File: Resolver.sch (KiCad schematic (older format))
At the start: 10 parts, among them U6 AD2S1200YSTZ, Y2 8.912 MHZ

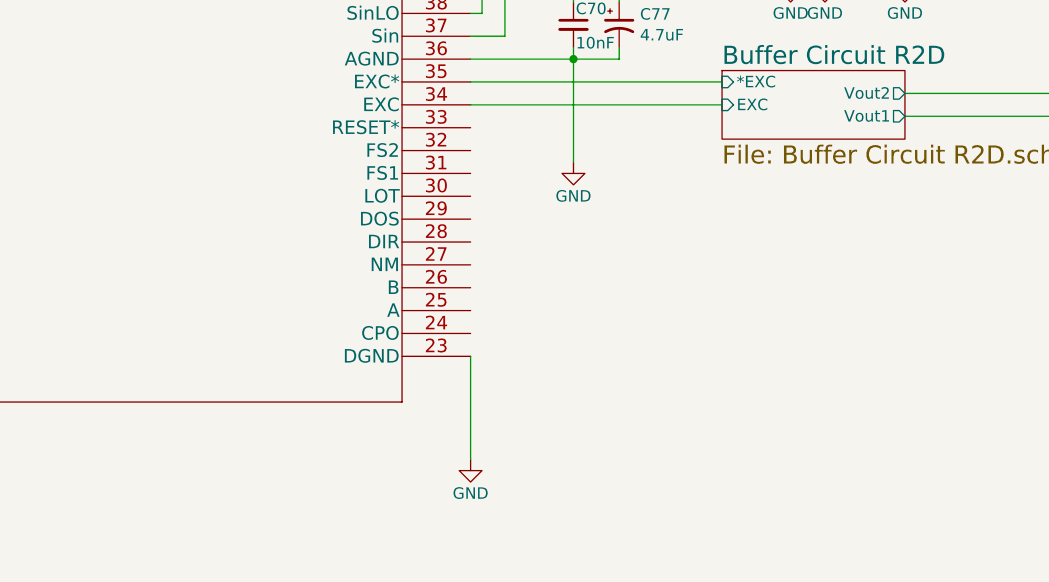
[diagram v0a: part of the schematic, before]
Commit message: continued R2D AS1200 has encoder-interface
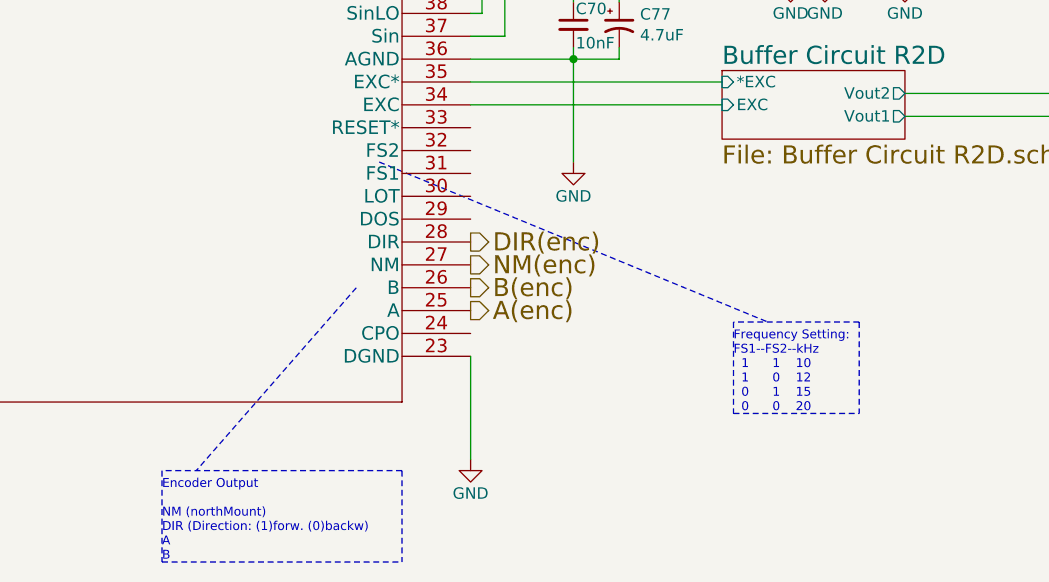
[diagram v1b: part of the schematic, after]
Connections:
- net A(enc): now reaches U6.25 (A)
- net B(enc): now reaches U6.26 (B)
- net NM(enc): now reaches U6.27 (NM)
- net DIR(enc): now reaches U6.28 (DIR)
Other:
- note added: "Encoder Output\n\nNM (northMount)\nDIR (Direction: (1)forw. (0)backw)\nA\nB"
- note added: "Frequency Setting:\nFS1--FS2--kHz\n 1 1 10\n 1 0 12\n 0 1 15\n 0 0 20"
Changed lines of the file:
@@
 P 5850 5350
 AR Path="/5895E6A0/5CAF8D8E" Ref="#PWR?"  Part="1"
-AR Path="/5C9D0FFC/5CAF8D8E" Ref="#PWR?"  Part="1"
-F 0 "#PWR?" H 5850 5100 50  0001 C CNN
+AR Path="/5C9D0FFC/5CAF8D8E" Ref="#PWR0138"  Part="1"
+F 0 "#PWR0138" H 5850 5100 50  0001 C CNN
 F 1 "GND" H 5850 5200 50  0000 C CNN
 F 2 "" H 5850 5350 50  0000 C CNN
@@
 Wire Wire Line
 	2150 3200 2850 3200
+Text Notes 7000 5150 0    39   ~ 0
+Frequency Setting:\nFS1--FS2--kHz\n  1      1    10\n  1      0    12\n  0      1    15\n  0      0    20
+Wire Notes Line
+	5450 4050 7150 4750
+Wire Notes Line
+	7000 5150 7550 5150
+Wire Notes Line
+	7550 4750 7000 4750
+Wire Notes Line
+	7000 4750 7000 5150
+Wire Notes Line
+	7550 4750 7550 5150
+Text Notes 4500 5800 0    39   ~ 0
+Encoder Output\n\nNM (northMount)\nDIR (Direction: (1)forw. (0)backw)\nA\nB
+Wire Notes Line
+	5350 4600 4650 5400
+Wire Notes Line
+	4500 5800 5550 5800
+Wire Notes Line
+	5550 5400 4500 5400
+Wire Notes Line
+	4500 5400 4500 5800
+Wire Notes Line
+	5550 5400 5550 5800
+Text HLabel 5850 4600 2    79   Output ~ 0
+B(enc)
+Text HLabel 5850 4500 2    79   Output ~ 0
+NM(enc)
+Text HLabel 5850 4400 2    79   Output ~ 0
+DIR(enc)
+Text HLabel 5850 4700 2    79   Output ~ 0
+A(enc)
 $EndSCHEMATC

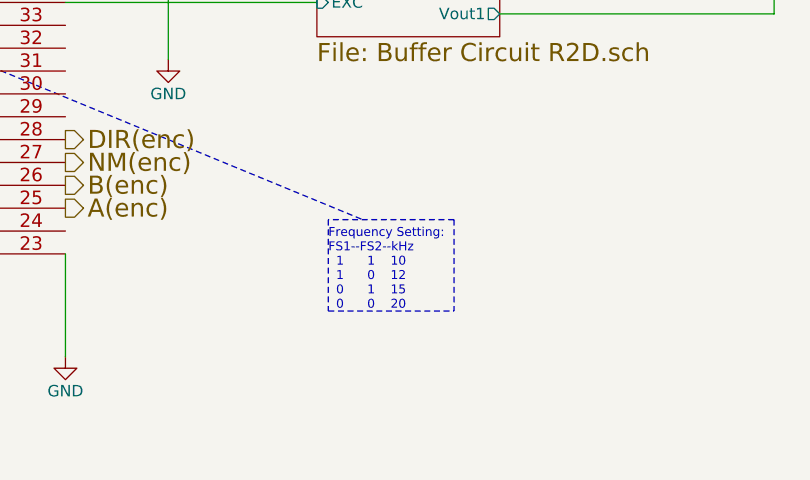
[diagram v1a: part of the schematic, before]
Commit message: continued Resolver continued Routing
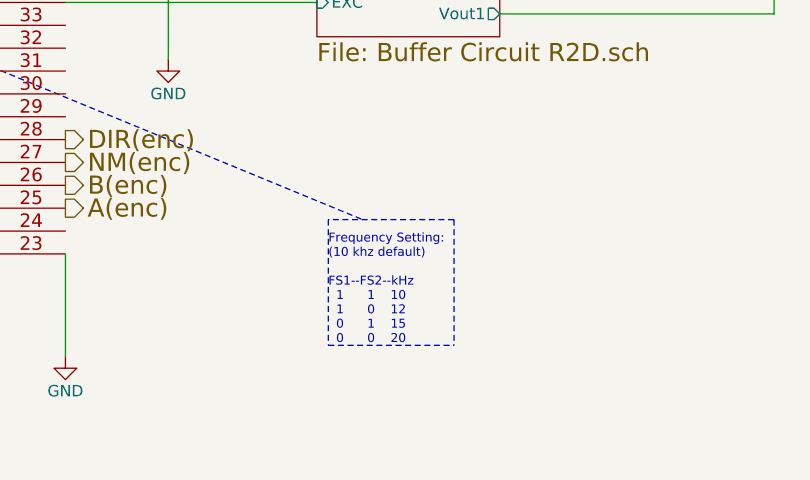
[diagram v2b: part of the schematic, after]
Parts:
- C74, C77: footprint Capacitor_SMD:C_0805_2012Metric -> Capacitor_Tantalum_SMD:CP_EIA-3216-12_Kemet-S
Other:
- note added: "Frequency Setting:\n(10 khz default)\n\nFS1--FS2--kHz\n 1 1 10\n 1 0 12\n 0 1 15\n 0 0 20"
- note removed: "Frequency Setting:\nFS1--FS2--kHz\n 1 1 10\n 1 0 12\n 0 1 15\n 0 0 20"
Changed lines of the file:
@@
 $Descr A4 11693 8268
 encoding utf-8
-Sheet 8 10
+Sheet 9 10
 Title ""
 Date ""
@@
 F 0 "C77" H 6591 3496 50  0000 L CNN
 F 1 "4.7uF" H 6591 3405 50  0000 L CNN
-F 2 "Capacitor_SMD:C_0805_2012Metric" H 6500 3450 50  0001 C CNN
+F 2 "Capacitor_Tantalum_SMD:CP_EIA-3216-12_Kemet-S" H 6500 3450 50  0001 C CNN
 F 3 "~" H 6500 3450 50  0001 C CNN
 	1    6500 3450
@@
 F 0 "C74" H 1441 4596 50  0000 L CNN
 F 1 "4.7uF" H 1441 4505 50  0000 L CNN
-F 2 "Capacitor_SMD:C_0805_2012Metric" H 1350 4550 50  0001 C CNN
+F 2 "Capacitor_Tantalum_SMD:CP_EIA-3216-12_Kemet-S" H 1350 4550 50  0001 C CNN
 F 3 "~" H 1350 4550 50  0001 C CNN
 	1    1350 4550
@@
 Wire Wire Line
 	2150 3200 2850 3200
-Text Notes 7000 5150 0    39   ~ 0
-Frequency Setting:\nFS1--FS2--kHz\n  1      1    10\n  1      0    12\n  0      1    15\n  0      0    20
+Text Notes 7000 5300 0    39   ~ 0
+Frequency Setting:\n(10 khz default)\n\nFS1--FS2--kHz\n  1      1    10\n  1      0    12\n  0      1    15\n  0      0    20
 Wire Notes Line
 	5450 4050 7150 4750
 Wire Notes Line
-	7000 5150 7550 5150
+	7000 5300 7550 5300
 Wire Notes Line
 	7550 4750 7000 4750
 Wire Notes Line
-	7000 4750 7000 5150
-Wire Notes Line
-	7550 4750 7550 5150
+	7000 4750 7000 5300
+Wire Notes Line
+	7550 4750 7550 5300
 Text Notes 4500 5800 0    39   ~ 0
 Encoder Output\n\nNM (northMount)\nDIR (Direction: (1)forw. (0)backw)\nA\nB

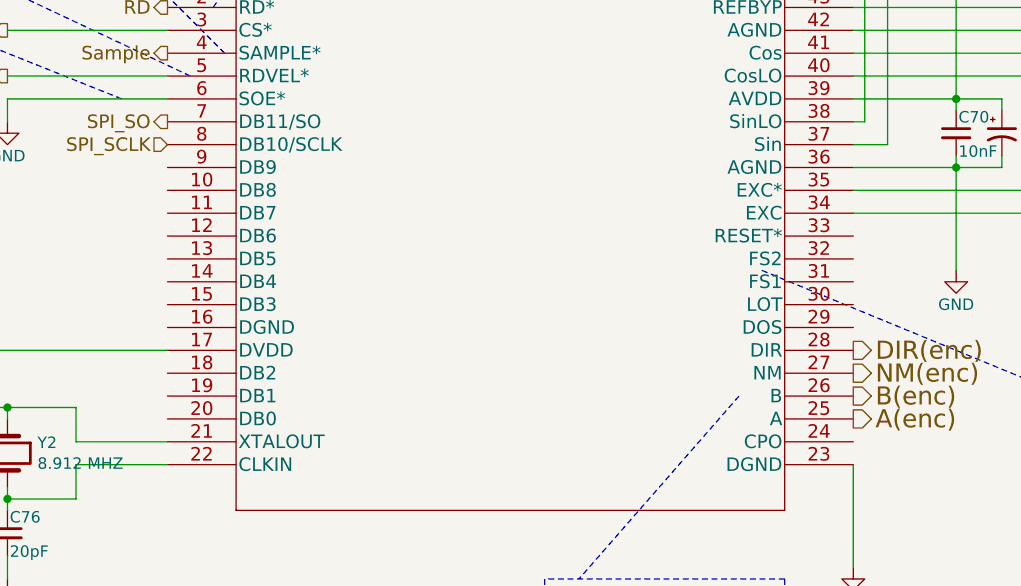
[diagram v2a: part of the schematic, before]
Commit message: continued routing, almost finished resolver. todo: -calc resistors for gain (resolver)       -Anfahren ohne encoder signal?!       -12V buffer R2D
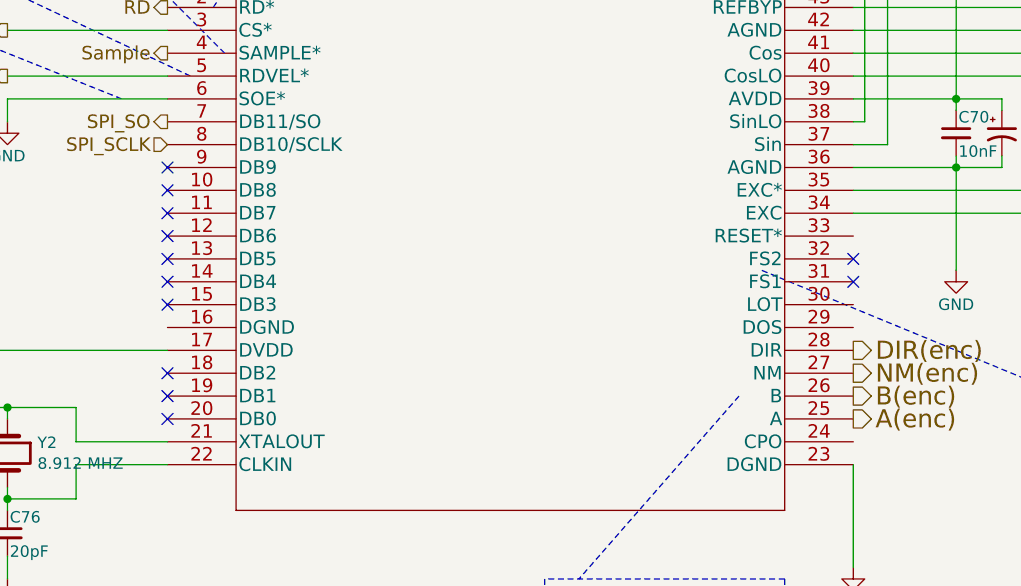
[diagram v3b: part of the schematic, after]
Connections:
- no-connect marks 0 -> 12
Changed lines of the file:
@@
 Text HLabel 5850 4700 2    79   Output ~ 0
 A(enc)
+NoConn ~ 2850 3600
+NoConn ~ 2850 3700
+NoConn ~ 2850 3800
+NoConn ~ 2850 3900
+NoConn ~ 2850 4000
+NoConn ~ 2850 4100
+NoConn ~ 2850 4200
+NoConn ~ 2850 4600
+NoConn ~ 2850 4700
+NoConn ~ 2850 4500
+NoConn ~ 5850 4000
+NoConn ~ 5850 4100
 $EndSCHEMATC

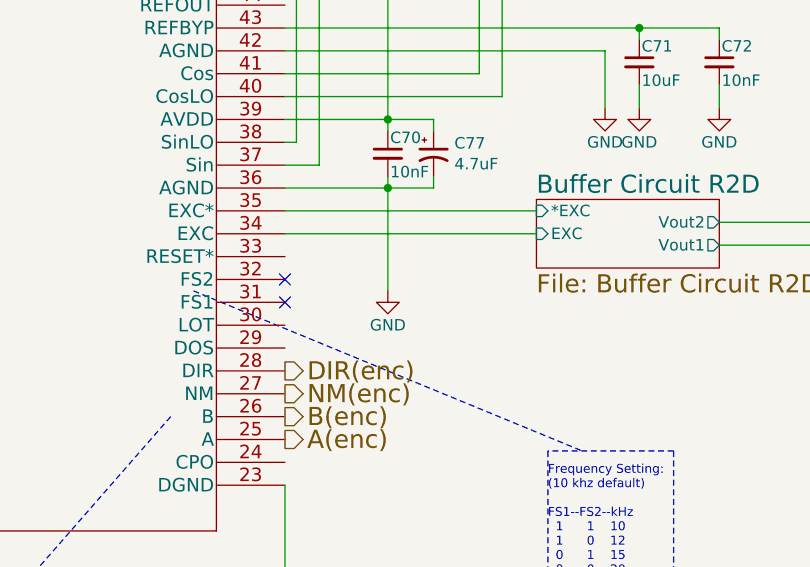
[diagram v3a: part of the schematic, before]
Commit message: Mäusepiano (for Piano-Beginner) Areas tidied up new Phase- and Batterie-Connector and Benchmark for Pressfit Hall-filter back on PCB solder-jumper for choice: Resolver or Hallfilter
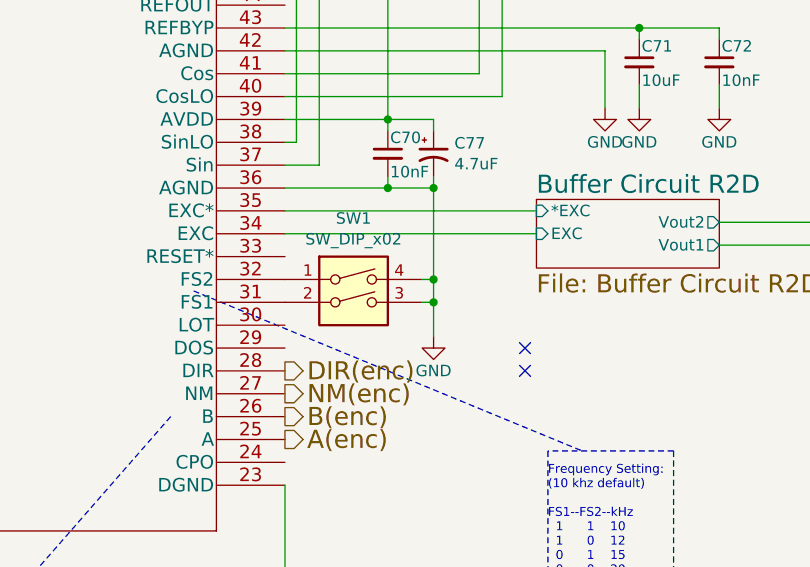
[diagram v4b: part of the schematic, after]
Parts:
- added SW1: SW_DIP_x02, Buttons_Switches_SMD:SW_DIP_x2_W5.08mm_Slide_Copal_CHS-A, symbol Switch:SW_DIP_x02
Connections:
- net GND: now also SW1.3, SW1.4
- net at U6.31 (FS1): now also SW1.2
- net at U6.32 (FS2): now also SW1.1
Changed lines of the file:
@@
 L Amalga_100-rescue:GND-power #PWR?
 U 1 1 5C9EA937
-P 6300 4050
+P 6500 4250
 AR Path="/5895E6A0/5C9EA937" Ref="#PWR?"  Part="1"
 AR Path="/5C9D0FFC/5C9EA937" Ref="#PWR0106"  Part="1"
-F 0 "#PWR0106" H 6300 3800 50  0001 C CNN
-F 1 "GND" H 6300 3900 50  0000 C CNN
-F 2 "" H 6300 4050 50  0000 C CNN
-F 3 "" H 6300 4050 50  0000 C CNN
-	1    6300 4050
+F 0 "#PWR0106" H 6500 4000 50  0001 C CNN
+F 1 "GND" H 6500 4100 50  0000 C CNN
+F 2 "" H 6500 4250 50  0000 C CNN
+F 3 "" H 6500 4250 50  0000 C CNN
+	1    6500 4250
 	1    0    0    -1
 $EndComp
@@
 $EndSheet
 Wire Wire Line
-	6300 4050 6300 3600
+	6500 4250 6500 4100
 Wire Wire Line
 	5850 3800 6950 3800
@@
 NoConn ~ 2850 4700
 NoConn ~ 2850 4500
-NoConn ~ 5850 4000
-NoConn ~ 5850 4100
+NoConn ~ 6900 4300
+NoConn ~ 6900 4400
+$Comp
+L Switch:SW_DIP_x02 SW1
+U 1 1 5CB84172
+P 6150 4100
+F 0 "SW1" H 6150 4467 50  0000 C CNN
+F 1 "SW_DIP_x02" H 6150 4376 50  0000 C CNN
+F 2 "Buttons_Switches_SMD:SW_DIP_x2_W5.08mm_Slide_Copal_CHS-A" H 6150 4100 50  0001 C CNN
+F 3 "" H 6150 4100 50  0001 C CNN
+	1    6150 4100
+	1    0    0    -1
+$EndComp
+Connection ~ 6500 3600
+Wire Wire Line
+	6450 4000 6500 4000
+Connection ~ 6500 4000
+Wire Wire Line
+	6500 4000 6500 3600
+Wire Wire Line
+	6450 4100 6500 4100
+Connection ~ 6500 4100
+Wire Wire Line
+	6500 4100 6500 4000
 $EndSCHEMATC

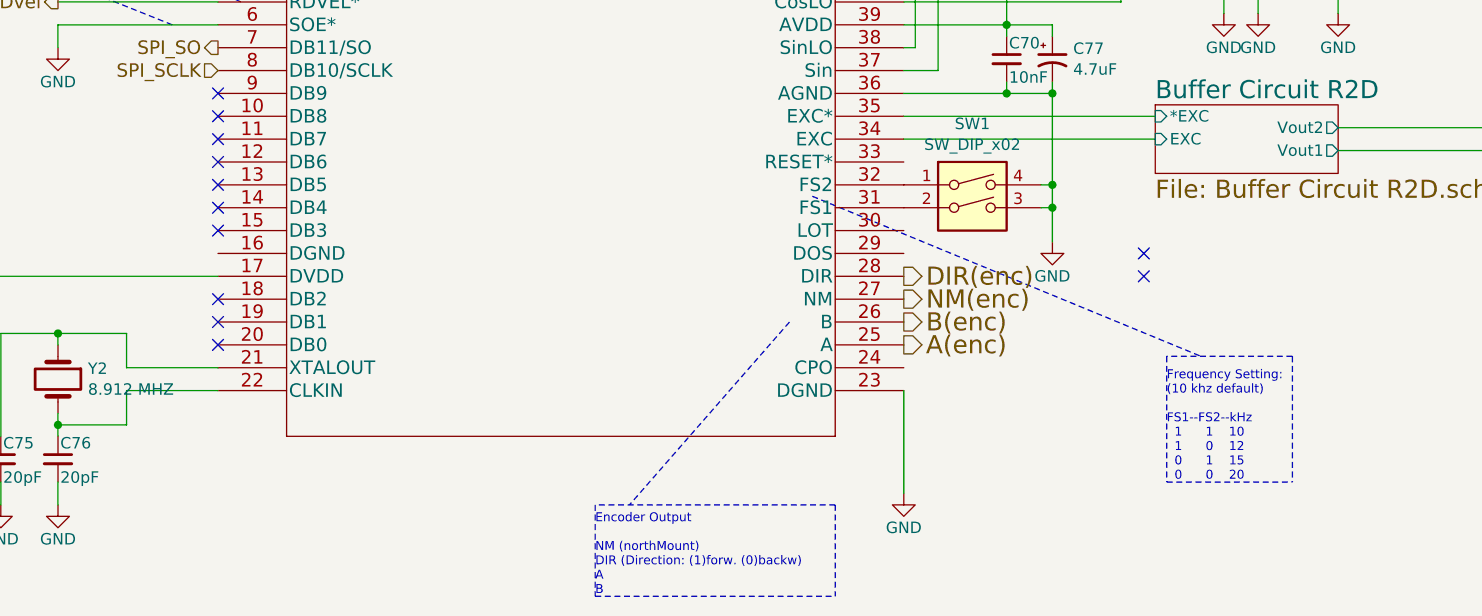
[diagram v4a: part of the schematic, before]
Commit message: -tidied up resolver circuit (need voltage detection on reset pin. >10µs, low active)
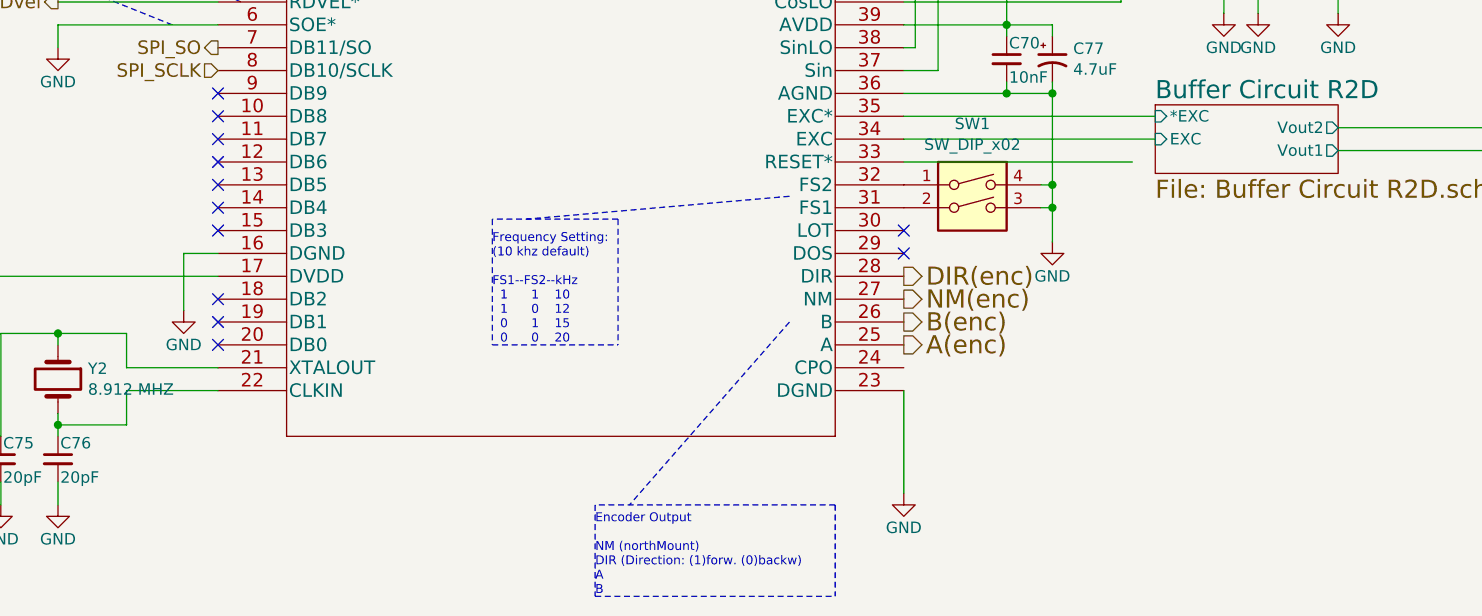
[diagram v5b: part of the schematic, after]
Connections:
- net GND: now also U6.16 (DGND)
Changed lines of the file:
@@
 EESchema Schematic File Version 4
 LIBS:Amalga_100-cache
-EELAYER 26 0
+EELAYER 29 0
 EELAYER END
 $Descr A4 11693 8268
@@
 Wire Wire Line
 	2150 3200 2850 3200
-Text Notes 7000 5300 0    39   ~ 0
+Text Notes 4050 4700 0    39   ~ 0
 Frequency Setting:\n(10 khz default)\n\nFS1--FS2--kHz\n  1      1    10\n  1      0    12\n  0      1    15\n  0      0    20
 Wire Notes Line
-	5450 4050 7150 4750
-Wire Notes Line
-	7000 5300 7550 5300
-Wire Notes Line
-	7550 4750 7000 4750
-Wire Notes Line
-	7000 4750 7000 5300
-Wire Notes Line
-	7550 4750 7550 5300
+	5350 4050 4200 4150
+Wire Notes Line
+	4050 4700 4600 4700
+Wire Notes Line
+	4600 4150 4050 4150
+Wire Notes Line
+	4050 4150 4050 4700
+Wire Notes Line
+	4600 4150 4600 4700
 Text Notes 4500 5800 0    39   ~ 0
 Encoder Output\n\nNM (northMount)\nDIR (Direction: (1)forw. (0)backw)\nA\nB
@@
 NoConn ~ 2850 4700
 NoConn ~ 2850 4500
-NoConn ~ 6900 4300
-NoConn ~ 6900 4400
+NoConn ~ 5850 4200
+NoConn ~ 5850 4300
 $Comp
 L Switch:SW_DIP_x02 SW1
@@
 Wire Wire Line
 	6500 4100 6500 4000
+Wire Wire Line
+	5850 3900 6850 3900
+Wire Wire Line
+	2850 4300 2700 4300
+$Comp
+L Amalga_100-rescue:GND-power #PWR?
+U 1 1 5CDC9AAC
+P 2700 4550
+AR Path="/5895E6A0/5CDC9AAC" Ref="#PWR?"  Part="1"
+AR Path="/5C9D0FFC/5CDC9AAC" Ref="#PWR0139"  Part="1"
+F 0 "#PWR0139" H 2700 4300 50  0001 C CNN
+F 1 "GND" H 2700 4400 50  0000 C CNN
+F 2 "" H 2700 4550 50  0000 C CNN
+F 3 "" H 2700 4550 50  0000 C CNN
+	1    2700 4550
+	1    0    0    -1
+$EndComp
+Wire Wire Line
+	2700 4300 2700 4550
 $EndSCHEMATC
